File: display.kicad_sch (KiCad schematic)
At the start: 17 parts, among them Q8 Q_NMOS_DGS, U12 E2266CS0C2

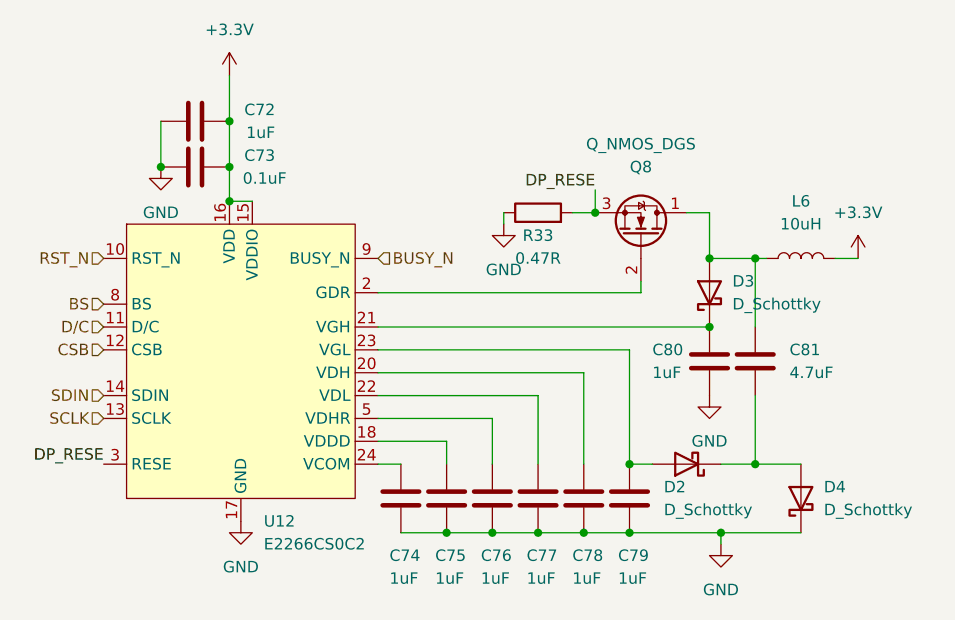
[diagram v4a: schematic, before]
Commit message: PI LC lowpass filter, added CP2012 reset, added connectors
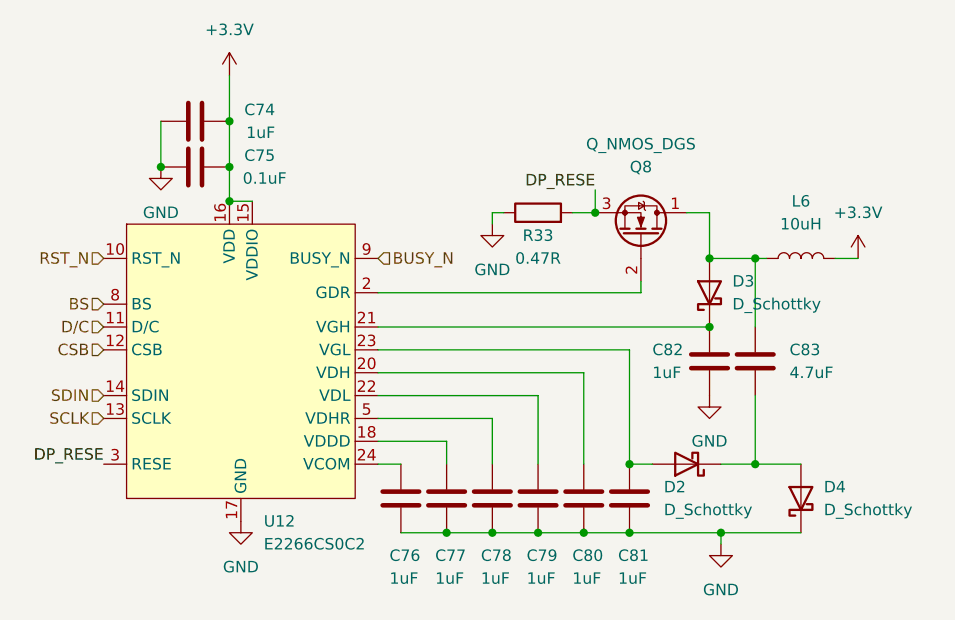
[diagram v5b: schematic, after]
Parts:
- renumbered C72 to C74, C73 to C75, C74 to C76, C75 to C77, C76 to C78, C77 to C79, C78 to C80, C79 to C81, C80 to C82, C81 to C83
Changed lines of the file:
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@@
     (stroke (width 0) (type default) (color 0 0 0 0))
   )
-  (wire (pts (xy 173.99 77.47) (xy 173.99 76.2))
+  (wire (pts (xy 172.72 77.47) (xy 172.72 76.2))
     (stroke (width 0) (type default) (color 0 0 0 0))
   )
@@
   )
   (wire (pts (xy 177.8 96.52) (xy 177.8 104.14))
+    (stroke (width 0) (type default) (color 0 0 0 0))
+  )
+  (wire (pts (xy 172.72 76.2) (xy 173.99 76.2))
     (stroke (width 0) (type default) (color 0 0 0 0))
   )
@@
   (symbol (lib_id "Device:C") (at 182.88 107.95 180) (unit 1)
     (in_bom yes) (on_board yes)
-    (property "Reference" "C78" (id 0) (at 181.61 114.3 0)
+    (property "Reference" "C80" (id 0) (at 181.61 114.3 0)
       (effects (font (size 1.27 1.27)) (justify right))
     )
@@
   (symbol (lib_id "power:GND") (at 196.85 96.52 0) (unit 1)
     (in_bom yes) (on_board yes) (fields_autoplaced)
-    (property "Reference" "#PWR095" (id 0) (at 196.85 102.87 0)
+    (property "Reference" "#PWR094" (id 0) (at 196.85 102.87 0)
       (effects (font (size 1.27 1.27)) hide)
     )
@@
   (symbol (lib_id "power:GND") (at 135.89 71.12 0) (unit 1)
     (in_bom yes) (on_board yes) (fields_autoplaced)
-    (property "Reference" "#PWR091" (id 0) (at 135.89 77.47 0)
+    (property "Reference" "#PWR090" (id 0) (at 135.89 77.47 0)
       (effects (font (size 1.27 1.27)) hide)
     )
@@
   (symbol (lib_id "power:GND") (at 144.78 110.49 0) (unit 1)
     (in_bom yes) (on_board yes) (fields_autoplaced)
-    (property "Reference" "#PWR093" (id 0) (at 144.78 116.84 0)
+    (property "Reference" "#PWR092" (id 0) (at 144.78 116.84 0)
       (effects (font (size 1.27 1.27)) hide)
     )
@@
   (symbol (lib_id "Device:C") (at 187.96 107.95 180) (unit 1)
     (in_bom yes) (on_board yes)
-    (property "Reference" "C79" (id 0) (at 186.69 114.3 0)
+    (property "Reference" "C81" (id 0) (at 186.69 114.3 0)
       (effects (font (size 1.27 1.27)) (justify right))
     )
@@
   (symbol (lib_id "power:+3.3V") (at 143.51 60.96 0) (unit 1)
     (in_bom yes) (on_board yes) (fields_autoplaced)
-    (property "Reference" "#PWR092" (id 0) (at 143.51 64.77 0)
+    (property "Reference" "#PWR091" (id 0) (at 143.51 64.77 0)
       (effects (font (size 1.27 1.27)) hide)
     )
@@
   (symbol (lib_id "Device:C") (at 162.56 107.95 180) (unit 1)
     (in_bom yes) (on_board yes)
-    (property "Reference" "C74" (id 0) (at 161.29 114.3 0)
+    (property "Reference" "C76" (id 0) (at 161.29 114.3 0)
       (effects (font (size 1.27 1.27)) (justify right))
     )
@@
   (symbol (lib_id "Device:C") (at 167.64 107.95 180) (unit 1)
     (in_bom yes) (on_board yes)
-    (property "Reference" "C75" (id 0) (at 166.37 114.3 0)
+    (property "Reference" "C77" (id 0) (at 166.37 114.3 0)
       (effects (font (size 1.27 1.27)) (justify right))
     )
@@
   (symbol (lib_id "Device:C") (at 139.7 71.12 270) (unit 1)
     (in_bom yes) (on_board yes)
-    (property "Reference" "C73" (id 0) (at 148.59 69.85 90)
+    (property "Reference" "C75" (id 0) (at 148.59 69.85 90)
       (effects (font (size 1.27 1.27)) (justify right))
     )
@@
   (symbol (lib_id "power:+3.3V") (at 213.36 81.28 0) (unit 1)
     (in_bom yes) (on_board yes) (fields_autoplaced)
-    (property "Reference" "#PWR097" (id 0) (at 213.36 85.09 0)
+    (property "Reference" "#PWR096" (id 0) (at 213.36 85.09 0)
       (effects (font (size 1.27 1.27)) hide)
     )
@@
     (pin "1")
   )
-  (symbol (lib_id "power:GND") (at 173.99 77.47 0) (unit 1)
-    (in_bom yes) (on_board yes) (fields_autoplaced)
-    (property "Reference" "#PWR094" (id 0) (at 173.99 83.82 0)
-      (effects (font (size 1.27 1.27)) hide)
-    )
-    (property "Value" "GND" (id 1) (at 173.99 82.55 0))
-    (property "Footprint" "" (id 2) (at 173.99 77.47 0)
-      (effects (font (size 1.27 1.27)) hide)
-    )
-    (property "Datasheet" "" (id 3) (at 173.99 77.47 0)
+  (symbol (lib_id "power:GND") (at 172.72 77.47 0) (unit 1)
+    (in_bom yes) (on_board yes) (fields_autoplaced)
+    (property "Reference" "#PWR093" (id 0) (at 172.72 83.82 0)
+      (effects (font (size 1.27 1.27)) hide)
+    )
+    (property "Value" "GND" (id 1) (at 172.72 82.55 0))
+    (property "Footprint" "" (id 2) (at 172.72 77.47 0)
+      (effects (font (size 1.27 1.27)) hide)
+    )
+    (property "Datasheet" "" (id 3) (at 172.72 77.47 0)
       (effects (font (size 1.27 1.27)) hide)
     )
@@
   (symbol (lib_id "Device:C") (at 139.7 66.04 270) (unit 1)
     (in_bom yes) (on_board yes)
-    (property "Reference" "C72" (id 0) (at 148.59 64.77 90)
+    (property "Reference" "C74" (id 0) (at 148.59 64.77 90)
       (effects (font (size 1.27 1.27)) (justify right))
     )
@@
   (symbol (lib_id "Device:C") (at 177.8 107.95 180) (unit 1)
     (in_bom yes) (on_board yes)
-    (property "Reference" "C77" (id 0) (at 176.53 114.3 0)
+    (property "Reference" "C79" (id 0) (at 176.53 114.3 0)
       (effects (font (size 1.27 1.27)) (justify right))
     )
@@
   (symbol (lib_id "Device:C") (at 172.72 107.95 180) (unit 1)
     (in_bom yes) (on_board yes)
-    (property "Reference" "C76" (id 0) (at 171.45 114.3 0)
+    (property "Reference" "C78" (id 0) (at 171.45 114.3 0)
       (effects (font (size 1.27 1.27)) (justify right))
     )
@@
   (symbol (lib_id "power:GND") (at 198.12 113.03 0) (unit 1)
     (in_bom yes) (on_board yes) (fields_autoplaced)
-    (property "Reference" "#PWR096" (id 0) (at 198.12 119.38 0)
+    (property "Reference" "#PWR095" (id 0) (at 198.12 119.38 0)
       (effects (font (size 1.27 1.27)) hide)
     )
@@
   (symbol (lib_id "Device:C") (at 196.85 92.71 180) (unit 1)
     (in_bom yes) (on_board yes)
-    (property "Reference" "C80" (id 0) (at 190.5 91.44 0)
+    (property "Reference" "C82" (id 0) (at 190.5 91.44 0)
       (effects (font (size 1.27 1.27)) (justify right))
     )
@@
   (symbol (lib_id "Device:C") (at 201.93 92.71 180) (unit 1)
     (in_bom yes) (on_board yes)
-    (property "Reference" "C81" (id 0) (at 205.74 91.44 0)
-      (effects (font (size 1.27 1.27)) (justify right))
-    )
+    (property "Reference" "C83" (id 0) (at 205.74 91.44 0)
+      (effects (font (size 1.27 1.27)) (justify right))
+    )

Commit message: datasheet checkout, added couple of capacitors for usb-c, groupd some scheatics
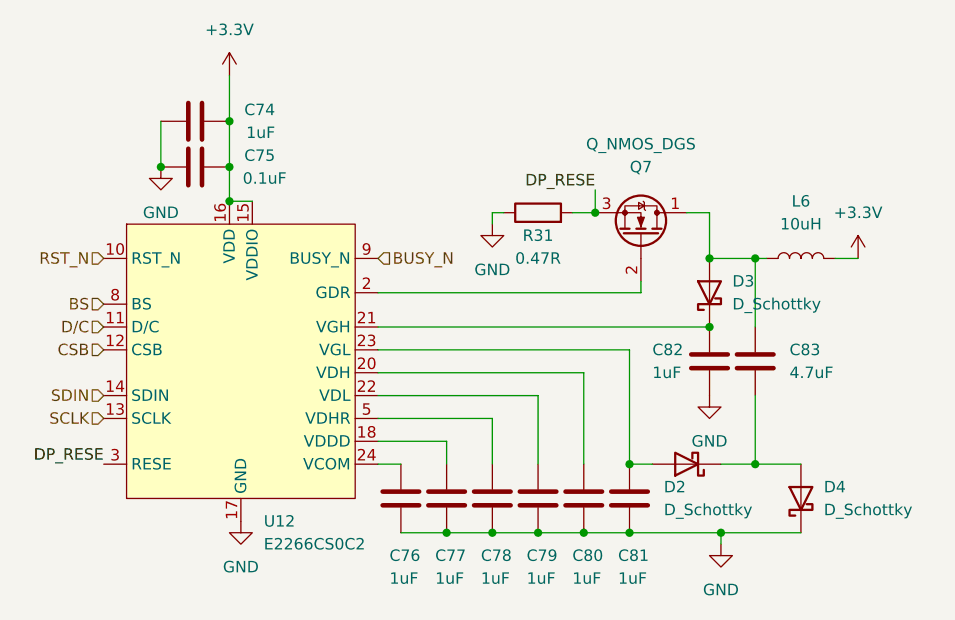
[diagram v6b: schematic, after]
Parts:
- renumbered Q8 to Q7, R33 to R31
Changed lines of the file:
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@@
   (symbol (lib_id "Device:Q_NMOS_DGS") (at 189.23 78.74 270) (mirror x) (unit 1)
     (in_bom yes) (on_board yes)
-    (property "Reference" "Q8" (id 0) (at 189.23 71.12 90))
+    (property "Reference" "Q7" (id 0) (at 189.23 71.12 90))
     (property "Value" "Q_NMOS_DGS" (id 1) (at 189.23 68.58 90))
     (property "Footprint" "" (id 2) (at 191.77 73.66 0)
@@
   (symbol (lib_id "power:GND") (at 196.85 96.52 0) (unit 1)
     (in_bom yes) (on_board yes) (fields_autoplaced)
-    (property "Reference" "#PWR094" (id 0) (at 196.85 102.87 0)
+    (property "Reference" "#PWR093" (id 0) (at 196.85 102.87 0)
       (effects (font (size 1.27 1.27)) hide)
     )
@@
   (symbol (lib_id "power:GND") (at 135.89 71.12 0) (unit 1)
     (in_bom yes) (on_board yes) (fields_autoplaced)
-    (property "Reference" "#PWR090" (id 0) (at 135.89 77.47 0)
+    (property "Reference" "#PWR089" (id 0) (at 135.89 77.47 0)
       (effects (font (size 1.27 1.27)) hide)
     )
@@
   (symbol (lib_id "power:GND") (at 144.78 110.49 0) (unit 1)
     (in_bom yes) (on_board yes) (fields_autoplaced)
-    (property "Reference" "#PWR092" (id 0) (at 144.78 116.84 0)
+    (property "Reference" "#PWR091" (id 0) (at 144.78 116.84 0)
       (effects (font (size 1.27 1.27)) hide)
     )
@@
   (symbol (lib_id "power:+3.3V") (at 143.51 60.96 0) (unit 1)
     (in_bom yes) (on_board yes) (fields_autoplaced)
-    (property "Reference" "#PWR091" (id 0) (at 143.51 64.77 0)
+    (property "Reference" "#PWR090" (id 0) (at 143.51 64.77 0)
       (effects (font (size 1.27 1.27)) hide)
     )
@@
   (symbol (lib_id "power:+3.3V") (at 213.36 81.28 0) (unit 1)
     (in_bom yes) (on_board yes) (fields_autoplaced)
-    (property "Reference" "#PWR096" (id 0) (at 213.36 85.09 0)
+    (property "Reference" "#PWR095" (id 0) (at 213.36 85.09 0)
       (effects (font (size 1.27 1.27)) hide)
     )
@@
   (symbol (lib_id "power:GND") (at 172.72 77.47 0) (unit 1)
     (in_bom yes) (on_board yes) (fields_autoplaced)
-    (property "Reference" "#PWR093" (id 0) (at 172.72 83.82 0)
+    (property "Reference" "#PWR092" (id 0) (at 172.72 83.82 0)
       (effects (font (size 1.27 1.27)) hide)
     )
@@
   (symbol (lib_id "Device:R") (at 177.8 76.2 90) (unit 1)
     (in_bom yes) (on_board yes)
-    (property "Reference" "R33" (id 0) (at 177.8 78.74 90))
+    (property "Reference" "R31" (id 0) (at 177.8 78.74 90))
     (property "Value" "0.47R" (id 1) (at 177.8 81.28 90))
     (property "Footprint" "" (id 2) (at 177.8 77.978 90)
@@
   (symbol (lib_id "power:GND") (at 198.12 113.03 0) (unit 1)
     (in_bom yes) (on_board yes) (fields_autoplaced)
-    (property "Reference" "#PWR095" (id 0) (at 198.12 119.38 0)
-      (effects (font (size 1.27 1.27)) hide)
-    )
+    (property "Reference" "#PWR094" (id 0) (at 198.12 119.38 0)
+      (effects (font (size 1.27 1.27)) hide)
+    )

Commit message: added nfc antenna components, added most of footprints
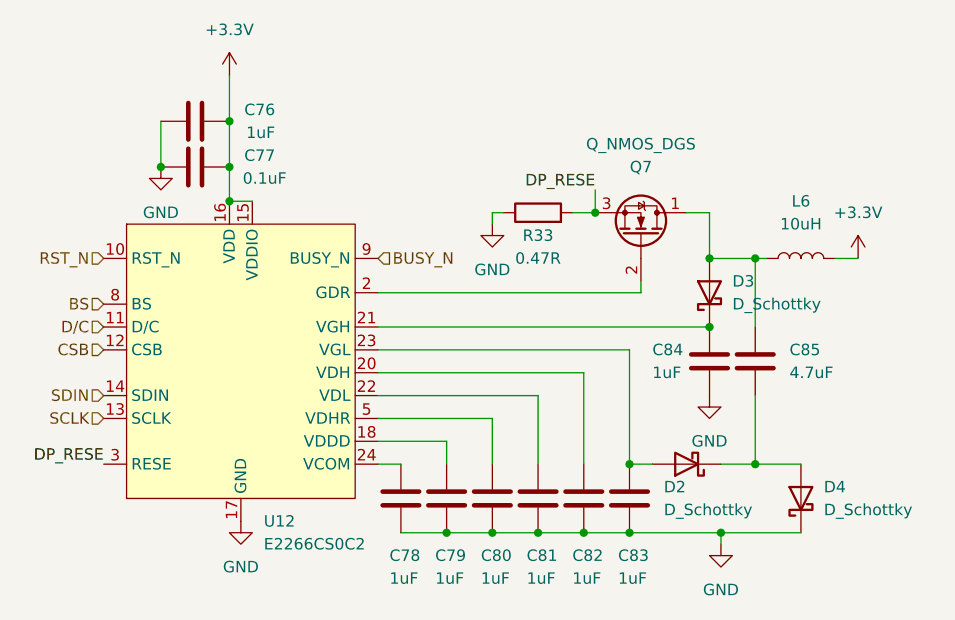
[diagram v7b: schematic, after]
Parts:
- C76: renamed from C74; footprint (none) -> Capacitor_SMD:C_0603_1608Metric_Pad1.08x0.95mm_HandSolder
- C77: renamed from C75; footprint (none) -> Capacitor_SMD:C_0603_1608Metric_Pad1.08x0.95mm_HandSolder
- C78: renamed from C76; footprint (none) -> Capacitor_SMD:C_0603_1608Metric_Pad1.08x0.95mm_HandSolder
- C79: renamed from C77; footprint (none) -> Capacitor_SMD:C_0603_1608Metric_Pad1.08x0.95mm_HandSolder
- C80: renamed from C78; footprint (none) -> Capacitor_SMD:C_0603_1608Metric_Pad1.08x0.95mm_HandSolder
- C81: renamed from C79; footprint (none) -> Capacitor_SMD:C_0603_1608Metric_Pad1.08x0.95mm_HandSolder
- C82: renamed from C80; footprint (none) -> Capacitor_SMD:C_0603_1608Metric_Pad1.08x0.95mm_HandSolder
- C83: renamed from C81; footprint (none) -> Capacitor_SMD:C_0603_1608Metric_Pad1.08x0.95mm_HandSolder
- C84: renamed from C82; footprint (none) -> Capacitor_SMD:C_0603_1608Metric_Pad1.08x0.95mm_HandSolder
- C85: renamed from C83; footprint (none) -> Capacitor_SMD:C_0603_1608Metric_Pad1.08x0.95mm_HandSolder
- R33: renamed from R31; footprint (none) -> Resistor_SMD:R_0603_1608Metric
- U12: footprint (none) -> airsoft_controller:FPC-24p-0.5
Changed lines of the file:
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@@
   (symbol (lib_id "Device:C") (at 182.88 107.95 180) (unit 1)
     (in_bom yes) (on_board yes)
-    (property "Reference" "C80" (id 0) (at 181.61 114.3 0)
+    (property "Reference" "C82" (id 0) (at 181.61 114.3 0)
       (effects (font (size 1.27 1.27)) (justify right))
     )
@@
       (effects (font (size 1.27 1.27)) (justify right))
     )
-    (property "Footprint" "" (id 2) (at 181.9148 104.14 0)
+    (property "Footprint" "Capacitor_SMD:C_0603_1608Metric_Pad1.08x0.95mm_HandSolder" (id 2) (at 181.9148 104.14 0)
       (effects (font (size 1.27 1.27)) hide)
     )
@@
   (symbol (lib_id "Device:C") (at 187.96 107.95 180) (unit 1)
     (in_bom yes) (on_board yes)
-    (property "Reference" "C81" (id 0) (at 186.69 114.3 0)
+    (property "Reference" "C83" (id 0) (at 186.69 114.3 0)
       (effects (font (size 1.27 1.27)) (justify right))
     )
@@
       (effects (font (size 1.27 1.27)) (justify right))
     )
-    (property "Footprint" "" (id 2) (at 186.9948 104.14 0)
+    (property "Footprint" "Capacitor_SMD:C_0603_1608Metric_Pad1.08x0.95mm_HandSolder" (id 2) (at 186.9948 104.14 0)
       (effects (font (size 1.27 1.27)) hide)
     )
@@
   (symbol (lib_id "Device:C") (at 162.56 107.95 180) (unit 1)
     (in_bom yes) (on_board yes)
-    (property "Reference" "C76" (id 0) (at 161.29 114.3 0)
+    (property "Reference" "C78" (id 0) (at 161.29 114.3 0)
       (effects (font (size 1.27 1.27)) (justify right))
     )
@@
       (effects (font (size 1.27 1.27)) (justify right))
     )
-    (property "Footprint" "" (id 2) (at 161.5948 104.14 0)
+    (property "Footprint" "Capacitor_SMD:C_0603_1608Metric_Pad1.08x0.95mm_HandSolder" (id 2) (at 161.5948 104.14 0)
       (effects (font (size 1.27 1.27)) hide)
     )
@@
   (symbol (lib_id "Device:C") (at 167.64 107.95 180) (unit 1)
     (in_bom yes) (on_board yes)
-    (property "Reference" "C77" (id 0) (at 166.37 114.3 0)
+    (property "Reference" "C79" (id 0) (at 166.37 114.3 0)
       (effects (font (size 1.27 1.27)) (justify right))
     )
@@
       (effects (font (size 1.27 1.27)) (justify right))
     )
-    (property "Footprint" "" (id 2) (at 166.6748 104.14 0)
+    (property "Footprint" "Capacitor_SMD:C_0603_1608Metric_Pad1.08x0.95mm_HandSolder" (id 2) (at 166.6748 104.14 0)
       (effects (font (size 1.27 1.27)) hide)
     )
@@
   (symbol (lib_id "Device:C") (at 139.7 71.12 270) (unit 1)
     (in_bom yes) (on_board yes)
-    (property "Reference" "C75" (id 0) (at 148.59 69.85 90)
+    (property "Reference" "C77" (id 0) (at 148.59 69.85 90)
       (effects (font (size 1.27 1.27)) (justify right))
     )
@@
       (effects (font (size 1.27 1.27)) (justify right))
     )
-    (property "Footprint" "" (id 2) (at 135.89 72.0852 0)
+    (property "Footprint" "Capacitor_SMD:C_0603_1608Metric_Pad1.08x0.95mm_HandSolder" (id 2) (at 135.89 72.0852 0)
       (effects (font (size 1.27 1.27)) hide)
     )
@@
   (symbol (lib_id "Device:C") (at 139.7 66.04 270) (unit 1)
     (in_bom yes) (on_board yes)
-    (property "Reference" "C74" (id 0) (at 148.59 64.77 90)
+    (property "Reference" "C76" (id 0) (at 148.59 64.77 90)
       (effects (font (size 1.27 1.27)) (justify right))
     )
@@
       (effects (font (size 1.27 1.27)) (justify right))
     )
-    (property "Footprint" "" (id 2) (at 135.89 67.0052 0)
+    (property "Footprint" "Capacitor_SMD:C_0603_1608Metric_Pad1.08x0.95mm_HandSolder" (id 2) (at 135.89 67.0052 0)
       (effects (font (size 1.27 1.27)) hide)
     )
@@
   (symbol (lib_id "Device:R") (at 177.8 76.2 90) (unit 1)
     (in_bom yes) (on_board yes)
-    (property "Reference" "R31" (id 0) (at 177.8 78.74 90))
+    (property "Reference" "R33" (id 0) (at 177.8 78.74 90))
     (property "Value" "0.47R" (id 1) (at 177.8 81.28 90))
-    (property "Footprint" "" (id 2) (at 177.8 77.978 90)
+    (property "Footprint" "Resistor_SMD:R_0603_1608Metric" (id 2) (at 177.8 77.978 90)
       (effects (font (size 1.27 1.27)) hide)
     )
@@
   (symbol (lib_id "Device:C") (at 177.8 107.95 180) (unit 1)
     (in_bom yes) (on_board yes)
-    (property "Reference" "C79" (id 0) (at 176.53 114.3 0)
+    (property "Reference" "C81" (id 0) (at 176.53 114.3 0)
       (effects (font (size 1.27 1.27)) (justify right))
     )
@@
       (effects (font (size 1.27 1.27)) (justify right))
     )
-    (property "Footprint" "" (id 2) (at 176.8348 104.14 0)
+    (property "Footprint" "Capacitor_SMD:C_0603_1608Metric_Pad1.08x0.95mm_HandSolder" (id 2) (at 176.8348 104.14 0)
       (effects (font (size 1.27 1.27)) hide)
     )
@@
   (symbol (lib_id "Device:C") (at 172.72 107.95 180) (unit 1)
     (in_bom yes) (on_board yes)
-    (property "Reference" "C78" (id 0) (at 171.45 114.3 0)
+    (property "Reference" "C80" (id 0) (at 171.45 114.3 0)
       (effects (font (size 1.27 1.27)) (justify right))
     )
@@
       (effects (font (size 1.27 1.27)) (justify right))
     )
-    (property "Footprint" "" (id 2) (at 171.7548 104.14 0)
+    (property "Footprint" "Capacitor_SMD:C_0603_1608Metric_Pad1.08x0.95mm_HandSolder" (id 2) (at 171.7548 104.14 0)
       (effects (font (size 1.27 1.27)) hide)
     )
@@
   (symbol (lib_id "Device:C") (at 196.85 92.71 180) (unit 1)
     (in_bom yes) (on_board yes)
-    (property "Reference" "C82" (id 0) (at 190.5 91.44 0)
+    (property "Reference" "C84" (id 0) (at 190.5 91.44 0)
       (effects (font (size 1.27 1.27)) (justify right))
     )
@@
       (effects (font (size 1.27 1.27)) (justify right))
     )
-    (property "Footprint" "" (id 2) (at 195.8848 88.9 0)
+    (property "Footprint" "Capacitor_SMD:C_0603_1608Metric_Pad1.08x0.95mm_HandSolder" (id 2) (at 195.8848 88.9 0)
       (effects (font (size 1.27 1.27)) hide)
     )
@@
   (symbol (lib_id "Device:C") (at 201.93 92.71 180) (unit 1)
     (in_bom yes) (on_board yes)
-    (property "Reference" "C83" (id 0) (at 205.74 91.44 0)
+    (property "Reference" "C85" (id 0) (at 205.74 91.44 0)
       (effects (font (size 1.27 1.27)) (justify right))
     )
@@
       (effects (font (size 1.27 1.27)) (justify right))
     )
-    (property "Footprint" "" (id 2) (at 200.9648 88.9 0)
+    (property "Footprint" "Capacitor_SMD:C_0603_1608Metric_Pad1.08x0.95mm_HandSolder" (id 2) (at 200.9648 88.9 0)
       (effects (font (size 1.27 1.27)) hide)
     )
@@
       (effects (font (size 1.27 1.27)) (justify left))
     )
-    (property "Footprint" "" (id 2) (at 144.78 92.71 0)
-      (effects (font (size 1.27 1.27)) hide)
-    )
+    (property "Footprint" "airsoft_controller:FPC-24p-0.5" (id 2) (at 144.78 92.71 0)
+      (effects (font (size 1.27 1.27)) hide)
+    )
